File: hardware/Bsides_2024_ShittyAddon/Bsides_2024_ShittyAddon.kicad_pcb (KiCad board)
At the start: 2 copper layers, 50.2 x 25.6 mm, 0 parts

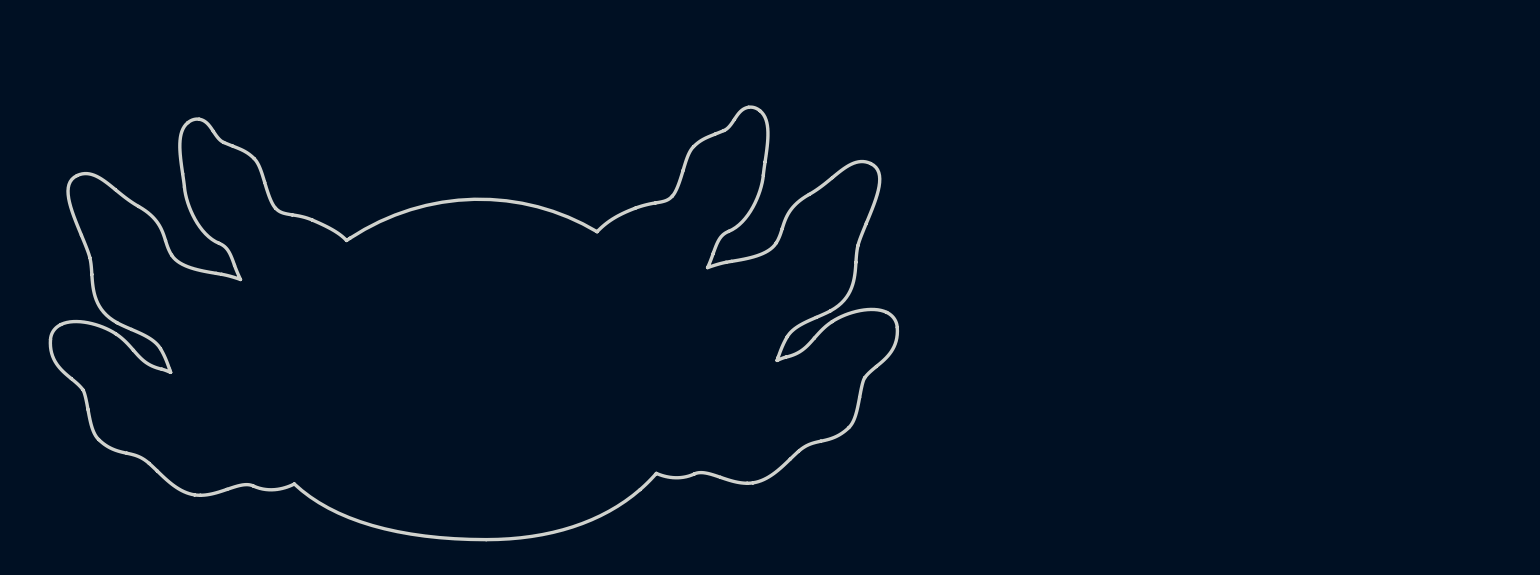
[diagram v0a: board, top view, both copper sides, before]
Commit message: feat(Hw): Start new floorplan
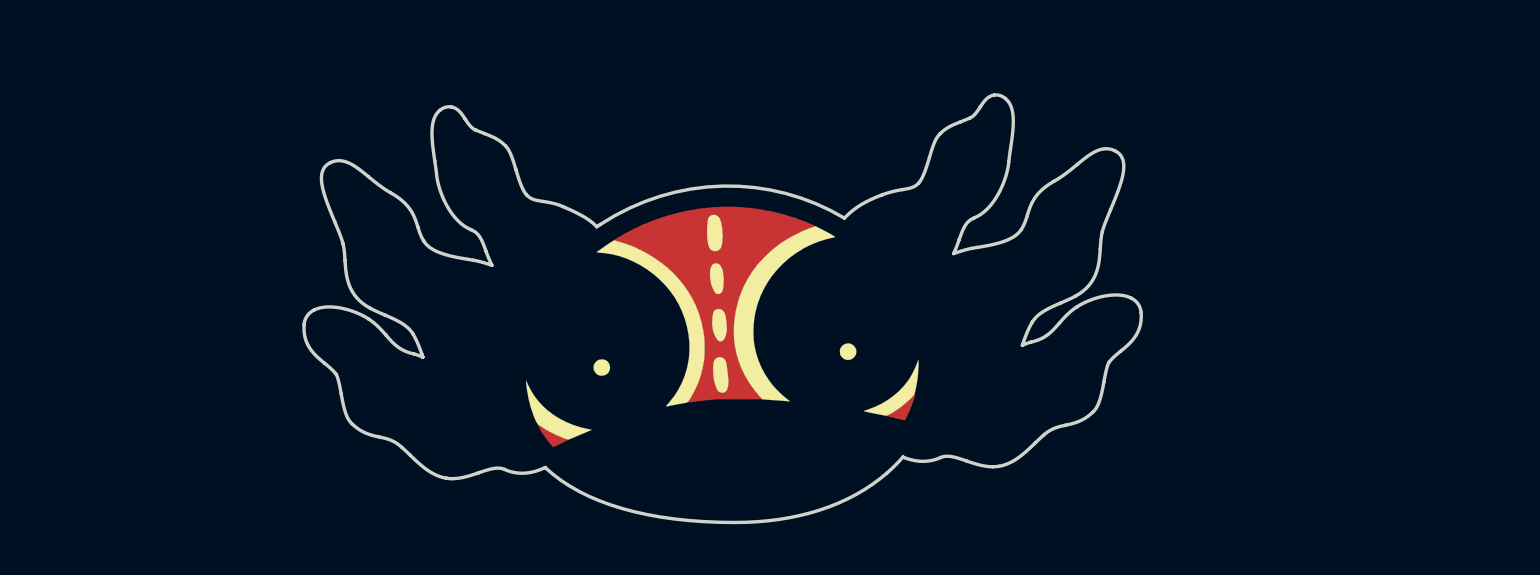
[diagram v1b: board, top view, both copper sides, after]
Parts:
- added Ref**: Val**, Footprints:Ajolote-bsidescdmx_A, F.Cu at (134.3, 71.9)
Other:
- board size 50.2 x 25.6 mm -> 49.7 x 25.4 mm

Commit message: feat(Hw): Update PCB
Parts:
- added C1: 0.1uF, Capacitor_SMD:C_0805_2012Metric, B.Cu at (134.8, 77.6)
- added D1: Green, LED_SMD:LED_0805_2012Metric, F.Cu at (119.8, 64.1)
- added D2: Red, LED_SMD:LED_0805_2012Metric, F.Cu at (113.8, 67.5)
- added D3: Blue, LED_SMD:LED_0805_2012Metric, F.Cu at (153.4, 69.0)
- added D4: Orange, LED_SMD:LED_0805_2012Metric, F.Cu at (95.2, 74.2)
- added D5: Yellow, LED_SMD:LED_0805_2012Metric, F.Cu at (148.4, 63.5)
- added J1: SWD, Footprints:PinHeader_1x04_P2.54mm_Vertical, B.Cu at (119.4, 79.8)
- added R1: 330R, Resistor_SMD:R_0805_2012Metric, B.Cu at (119.8, 64.2)
- added R2: 330R, Resistor_SMD:R_0805_2012Metric, B.Cu at (179.3, 56.2)
- added R3: 330R, Resistor_SMD:R_0805_2012Metric, B.Cu at (179.3, 59.2)
- added R4: 330R, Resistor_SMD:R_0805_2012Metric, B.Cu at (179.3, 62.1)
- added R5: 330R, Resistor_SMD:R_0805_2012Metric, B.Cu at (179.3, 65.1)
- added U1: PY32F002AA15M6TU, Footprints:PY32F002AA15M, B.Cu at (134.7, 81.7)

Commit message: feat(Hw): Update PCB
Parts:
- removed D4: Orange, LED_SMD:LED_0805_2012Metric
- removed R4: 330R, Resistor_SMD:R_0805_2012Metric
- moved R2 66.3 mm to (114.2, 68.2), turned to 110 degrees
- moved R5 30.7 mm to (148.7, 63.5), turned to 60 degrees
- moved R3 26.3 mm to (154.4, 67.5), turned to 70 degrees
- moved D3 1.80 mm to (154.4, 67.5), turned to -110 degrees
- moved D2 0.84 mm to (114.2, 68.2), turned to -70 degrees
- moved D5 0.27 mm to (148.7, 63.5), turned to -120 degrees

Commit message: feat(Hw): Update PCB
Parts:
- removed J1: SWD, Footprints:PinHeader_1x04_P2.54mm_Vertical
- added J2: Conn_02x03_Odd_Even, Footprints:B-2100N06P-B111_CKM, B.Cu at (137.1, 73.7)
- moved C1 8.39 mm to (127.4, 81.6)
- moved U1 0.97 mm to (134.7, 80.7), turned to 0 degrees
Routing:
- added copper zone on F.Cu, net (none)

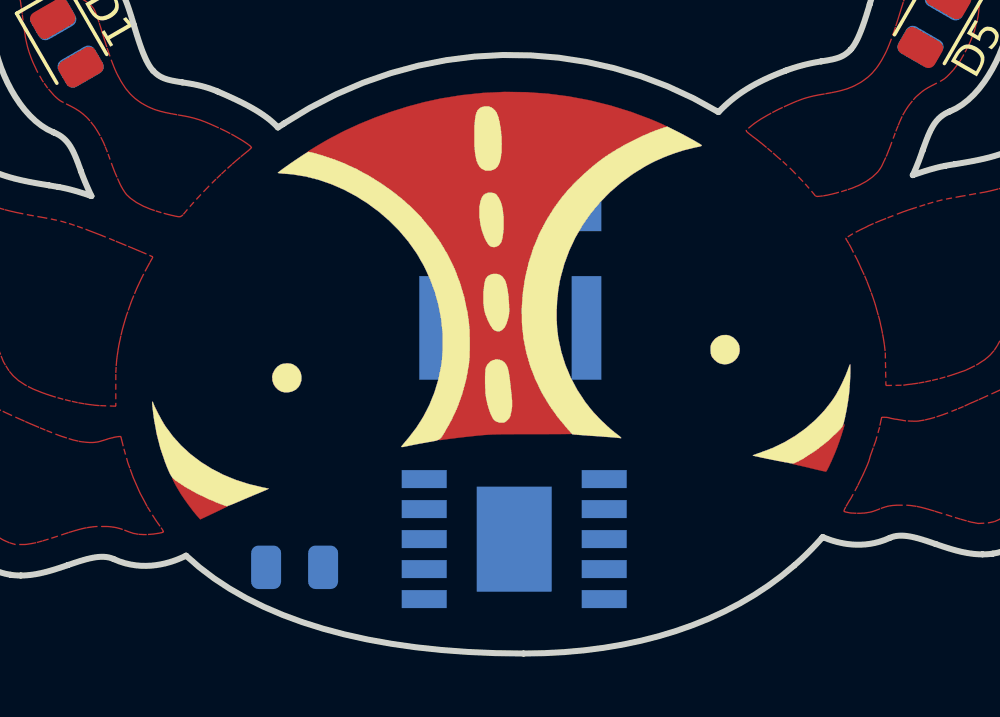
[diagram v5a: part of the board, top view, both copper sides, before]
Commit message: feat(Hw): Update route
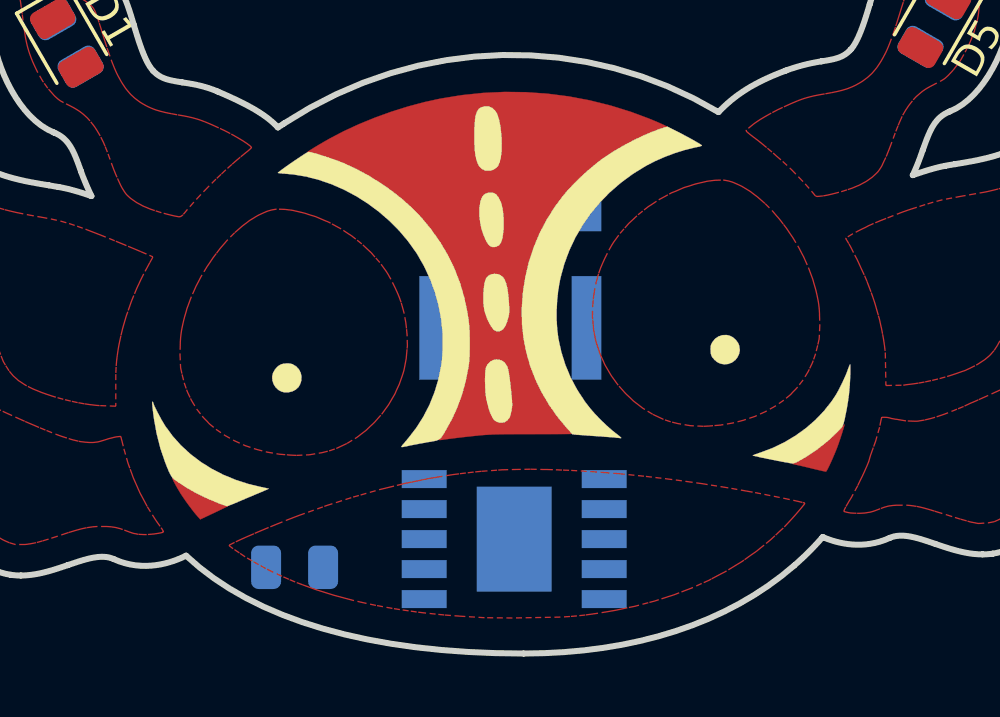
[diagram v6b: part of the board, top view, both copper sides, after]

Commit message: Update route and schematic
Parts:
- moved C1 0.72 mm to (128.1, 81.4), turned to 90 degrees
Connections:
- D2 pad 2: /PA7 -> /PF0
- D3 pad 2: /PA1 -> /PA7
- J2 pad 3: unconnected-(J2-Pin_3-Pad3) -> /PA1
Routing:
- net /PF0: track 0.00 -> 30.1 mm, vias 0 -> 1
- net /PA7: track 0.00 -> 28.8 mm, vias 0 -> 3
- net +3.3V: track 0.00 -> 27.3 mm, vias 0 -> 2
- net /PA5: track 0.00 -> 26.1 mm, vias 0 -> 1
- net /PA6: track 0.00 -> 23.2 mm, vias 0 -> 3
- net /SWCLK: track 0.00 -> 18.5 mm
- net GND: track 0.00 -> 11.9 mm, vias 0 -> 8
- net /SWDIO: track 0.00 -> 11.6 mm
- net /PA1: track 0.00 -> 7.37 mm
- net Net-(D3-K): track 0.00 -> 3.46 mm, vias 0 -> 1
- net Net-(D2-K): track 0.00 -> 3.24 mm, vias 0 -> 1
- net Net-(D5-K): track 0.00 -> 3.05 mm, vias 0 -> 1
- net Net-(D1-K): track 0.00 -> 2.78 mm, vias 0 -> 1
- added copper zone on B.Cu, net GND
- added copper zone on F.Cu, net GND
- removed copper zone on F.Cu, net (none)

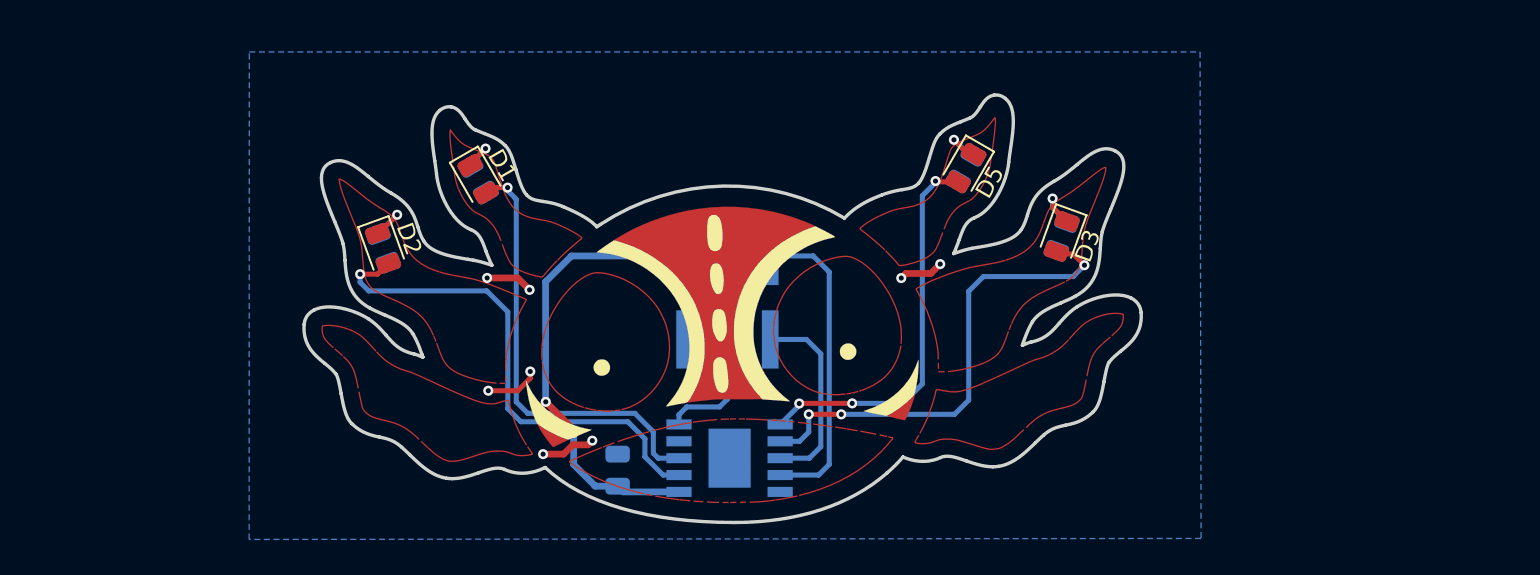
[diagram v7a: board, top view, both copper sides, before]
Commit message: feat(Hw): Update route
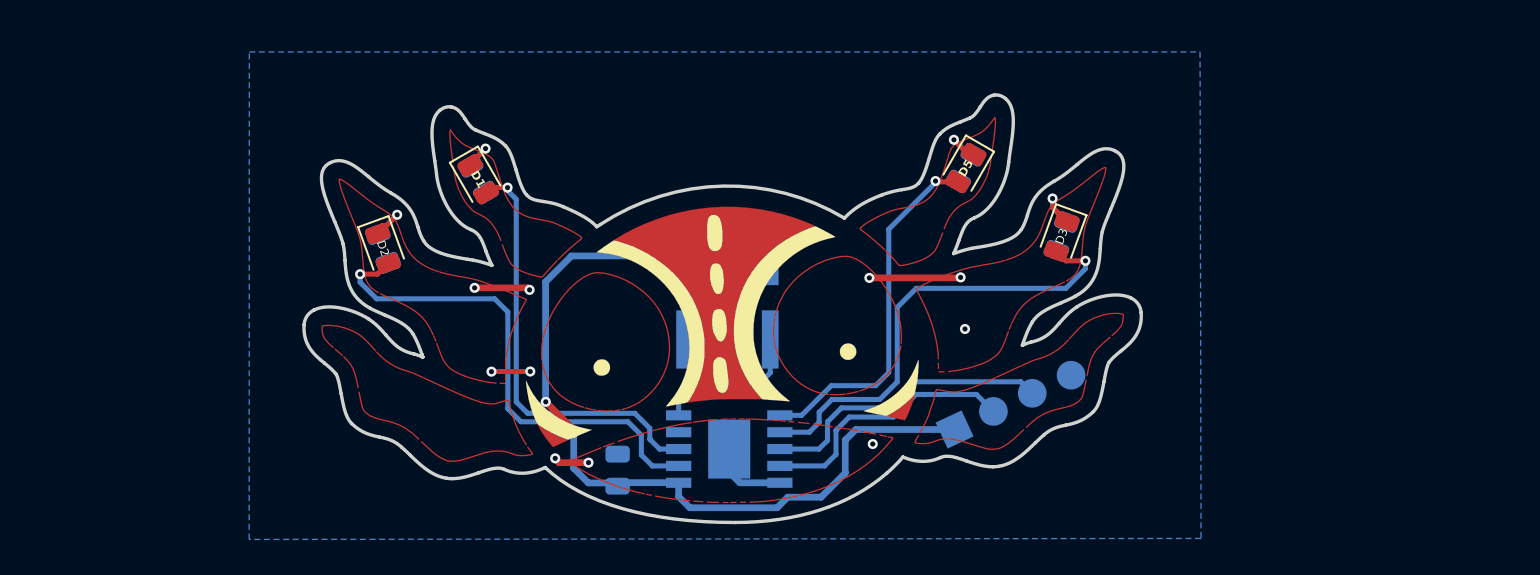
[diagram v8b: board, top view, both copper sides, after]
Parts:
- added J1: SWD, Footprints:PinHeader_1x04_P2.54mm_Vertical, B.Cu at (148.1, 79.0)
- moved U1 0.54 mm to (134.7, 80.2)
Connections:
- J2 pad 1: /SWDIO -> /PA1
- J2 pad 2: /SWCLK -> unconnected-(J2-Pin_2-Pad2)
- J2 pad 3: /PA1 -> unconnected-(J2-Pin_3-Pad3)
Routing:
- net +3.3V: track 27.3 -> 47.9 mm
- net /SWDIO: track 11.6 -> 17.6 mm
- net GND: track 11.9 -> 17.8 mm, vias 8 -> 10
- net /SWCLK: track 18.5 -> 15.7 mm
- net /PA6: track 23.2 -> 21.4 mm, vias 3 -> 1
- net /PA1: track 7.37 -> 9.03 mm
- net /PA7: track 28.8 -> 27.5 mm, vias 3 -> 1
- net /PA5: track 26.1 -> 25.5 mm
